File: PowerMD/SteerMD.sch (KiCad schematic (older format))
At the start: 202 parts, among them P1 SWD, P10 OUT_1, P11 ENC_0, P13 ENC_1, P14 I/O_1, P15 OUT_0, P3 CAN, P4 CAN, P5 SERIAL, P6 I/O_0, P7 FAN, P8 BATT_IN, P9 BATT_IN, Q1 MOSFET_N, Q2 MOSFET_N, Q3 MOSFET_N, Q4 MOSFET_N, Q5 MOSFET_N, Q6 MOSFET_N, Q7 MOSFET_N, Q8 MOSFET_N, SW1 RST, SW3 SW0, SW4 SW1, U1 MAX3051, U10 ACS758, U11 POWER_ON, U12 SI8274, U13 ACS758, U14 SI8274, U15 AZ1086H, U16 LOGO, U19 ADRESS, U2 AP3211, U3 STM32F405RG, U4 SI8274, U5 SI8900, U6 ADC_~RST, U7 BD9G101G, U8 SI8274, U9 BD33FA1, Y1 8MHz

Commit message: サーミスタのピンアサインの決定
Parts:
- added C53, C54, C58, C59: 0.1u, Capacitor_SMD:C_0603_1608Metric, symbol SteerMD-rescue:C-Device-MD_Enbarr_x2-rescue-F4_CAN_DCMD-rescue
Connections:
- net Current0: now also U3.25 (PC5/ADC12_IN15); no longer U3.11 (PC3/ADC12_IN13)
- net Current1: now also U3.24 (PC4/ADC12_IN14); no longer U3.10 (PC2/ADC12_IN12)
- net GND: now also C53.2, C54.2, C58.2, C59.2
- net LED0: no longer U3.22 (ADC12_IN6/TIM3_CH1/TIM13_CH1/PA6)
- net LED1: no longer U3.23 (ADC12_IN7/TIM1_CH1N/TIM8_CH1N/TIM14_CH1/TIM3_CH2/PA7)
- net LED2: no longer U3.24 (PC4/ADC12_IN14)
- net LED3: no longer U3.25 (PC5/ADC12_IN15)
- net Motor0L_Tmp: now also U3.8 (PC0/ADC12_IN10), C53.1
- net Motor0R_Tmp: now also U3.9 (PC1/ADC12_IN11), C58.1
- net Motor1L_Tmp: now also U3.10 (PC2/ADC12_IN12), C54.1
- net Motor1R_Tmp: now also U3.11 (PC3/ADC12_IN13), C59.1
- net LED4: no longer names the net of U3.26 (ADC12_IN8/TIM1_CH2N/TIM8_CH2N/TIM3_CH3/PB0)
- removed net Motor1_Tmp: U3.8 (PC0/ADC12_IN10), U3.9 (PC1/ADC12_IN11)
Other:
- moved on the sheet: R52, R67, R68, R69, TH1, TH2, TH3, TH4

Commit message: パワミMD
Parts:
- C34: footprint Capacitor_THT:CP_Radial_D10.0mm_P5.00mm -> Capacitor_THT:C_Radial_D12.5mm_H25.0mm_P5.00mm
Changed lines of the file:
@@
 F 0 "C34" H 10665 971 50  0000 L CNN
 F 1 "1500u" H 10665 880 50  0000 L CNN
-F 2 "Capacitor_THT:CP_Radial_D10.0mm_P5.00mm" H 10550 925 50  0001 C CNN
+F 2 "Capacitor_THT:C_Radial_D12.5mm_H25.0mm_P5.00mm" H 10550 925 50  0001 C CNN
 F 3 "~" H 10550 925 50  0001 C CNN
 	1    10550 925

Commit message: ピン配置王幅変更
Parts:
- added C60: 0.1u, Capacitor_SMD:C_0603_1608Metric, symbol SteerMD-rescue:C-Device-MD_Enbarr_x2-rescue-F4_CAN_DCMD-rescue
- added R70: FILTER, Resistor_SMD:R_0603_1608Metric, symbol SteerMD-rescue:R-Device-MD_Enbarr_x2-rescue-F4_CAN_DCMD-rescue
- added TH5: Thermistor, Capacitor_SMD:C_0603_1608Metric, symbol Device:Thermistor
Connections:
- net +3V3: now also TH5.1
- net ADR_1: no longer U3.4 (PC15/OSC32_OUT)
- net ADR_2: no longer U3.2 (PC13)
- net ADR_4: no longer U3.3 (PC14/OSC32_IN)
- net ADR_8: no longer U3.58 (TIM4_CH1/CAN2_TX/USART1_TX/PB6)
- net Current0: no longer U3.25 (PC5/ADC12_IN15)
- net Current1: no longer U3.24 (PC4/ADC12_IN14)
- net GND: now also C60.2, R70.2
- net Motor0L_Tmp: now also U3.9 (PC1/ADC12_IN11); no longer U3.8 (PC0/ADC12_IN10)
- net Motor0R_Tmp: now also U3.8 (PC0/ADC12_IN10); no longer U3.9 (PC1/ADC12_IN11)
- net Motor1L_Tmp: now also U3.25 (PC5/ADC12_IN15); no longer U3.10 (PC2/ADC12_IN12)
- net Motor1R_Tmp: now also U3.26 (ADC12_IN8/TIM1_CH2N/TIM8_CH2N/TIM3_CH3/PB0); no longer U3.11 (PC3/ADC12_IN13)
- net SW0: no longer U3.27 (ADC12_IN9/TIM1_CH3N/TIM8_CH3N/TIM3_CH4/PB1)
- net SW1: no longer U3.29 (USART3_TX/TIM2_CH3/PB10)
- net PA12: now reaches U3.45 (CAN1_TX/PA12)
- net PA12: now also U6.1
- net PA11: no longer names the net of U3.44 (CAN1_RX/TIM1_CH4/PA11)
- net PA11: no longer U6.1
- net PA15: no longer names the net of U3.50 (TIM2_CH1_ETR/PA15)
- net PA4 renamed IO_0
- net IO_0: no longer U3.20 (ADC12_IN4/PA4)
- net PA5: no longer names the net of U3.21 (ADC12_IN5/TIM2_CH1_ETR/TIM8_CH1N/PA5)
- net PA5: no longer P14.3 (P3)
- new net IO_1: P14.3 (P3)
- new net Substrate_Temp: C60.1, R70.1, TH5.2, U3.20 (ADC12_IN4/PA4)
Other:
- moved on the sheet: C53, C54, C58, C59, R52, R67, R68, R69, TH1, TH2, TH3, TH4

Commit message: MD
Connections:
- net ADR_1: now also U3.21 (ADC12_IN5/TIM2_CH1_ETR/TIM8_CH1N/PA5)
- net ADR_2: now also U3.23 (ADC12_IN7/TIM1_CH1N/TIM8_CH1N/TIM14_CH1/TIM3_CH2/PA7)
- net ADR_4: now also U3.22 (ADC12_IN6/TIM3_CH1/TIM13_CH1/PA6)
- net ADR_8: now also U3.27 (ADC12_IN9/TIM1_CH3N/TIM8_CH3N/TIM3_CH4/PB1)
- net Current0: now also U3.10 (PC2/ADC12_IN12)
- net Current1: now also U3.24 (PC4/ADC12_IN14)
- net LED0: now also U3.50 (TIM2_CH1_ETR/PA15)
- net LED1: now also U3.51 (PC10/UART4_TX/USART3_TX)
- net LED2: now also U3.52 (PC11/UART4_RX/USART3_RX)
- net LED3: now also U3.53 (PC12/UART5_TX)
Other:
- note added: "Filter:10kohm"
- note added: "Filter:3ohm"
- moved on the sheet: C15, C16, C26, C44, C55, D39, D7, D8, D9, P11, P13, P14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

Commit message: MDにモータ駆動用のファンぽーとをつけた
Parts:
- added P2: MOTOR_COOLING, Mizz_lib:XA_4L, symbol SteerMD-rescue:CONN_01X04-conn-MD_Enbarr_x2-rescue-F4_CAN_DCMD-rescue
- added R71, R72: 12, Mizz_lib:R_2812, symbol SteerMD-rescue:R-Device-MD_Enbarr_x2-rescue-F4_CAN_DCMD-rescue
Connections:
- net +12V: now also R71.2, R72.2
- net GND: now also P2.1 (P1), P2.3 (P3)
- net Motor1L_Tmp: no longer U3.25 (PC5/ADC12_IN15)
- net Motor1R_Tmp: now also U3.25 (PC5/ADC12_IN15); no longer U3.26 (ADC12_IN8/TIM1_CH2N/TIM8_CH2N/TIM3_CH3/PB0)
- net TIM4_CH1: now reaches U3.58 (TIM4_CH1/CAN2_TX/USART1_TX/PB6)
- net TIM4_CH1: now also R46.2
- net TIM4_CH2: now reaches U3.59 (USART1_RX/TIM4_CH2/PB7)
- net TIM4_CH2: now also R50.2
- net TIM5_CH1: no longer names the net of U3.14 (UART4_TX/TIM2_CH1_ETR/ADC12_IN0/TIM5_CH1/PA0)
- net TIM5_CH1: no longer R46.2
- net TIM5_CH2: no longer names the net of U3.15 (UART4_RX/ADC12_IN1/TIM5_CH2/TIM2_CH2/PA1)
- net TIM5_CH2: no longer R50.2
- new net: P2.2 (P2), R71.1
- new net: P2.4 (P4), R72.1
- new net Motor1l_Tmp: U3.26 (ADC12_IN8/TIM1_CH2N/TIM8_CH2N/TIM3_CH3/PB0)
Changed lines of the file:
@@
 Text Label 8250 900  2    50   ~ 0
 PA12
-Text Label 6900 6450 0    50   ~ 0
-PWM1_R
-Text Label 6900 6650 0    50   ~ 0
-PWM1_L
 Text Label 6900 6550 0    50   ~ 0
 EN1
@@
 	1    0    0    -1
 $EndComp
-Text Label 5350 9600 2    50   ~ 0
-TIM5_CH2
-Text Label 5350 9700 2    50   ~ 0
-TIM5_CH1
 $Comp
 L SteerMD-rescue:R-Device-MD_Enbarr_x2-rescue-F4_CAN_DCMD-rescue R24
@@
 Text Label 8125 4850 0    50   ~ 0
 SW1
-Text Label 6900 3450 0    50   ~ 0
-TIM5_CH1
-Text Label 6900 3550 0    50   ~ 0
-TIM5_CH2
 $Comp
 L SteerMD-rescue:CONN_01X03-conn-MD_Enbarr_x2-rescue-F4_CAN_DCMD-rescue P14
@@
 Motor0L_Tmp
 Text Label 2500 5650 2    50   ~ 0
-Motor1L_Tmp
-Text Label 6900 5150 0    50   ~ 0
 Motor1R_Tmp
+Text Label 6900 5150 0    50   ~ 0
+Motor1l_Tmp
 $Comp
 L Device:Thermistor TH5
@@
 Text Notes 7675 6050 0    50   ~ 0
 Filter:10kohm
+Text Label 6900 5850 0    50   ~ 0
+TIM4_CH2
+Text Label 6900 5750 0    50   ~ 0
+TIM4_CH1
+Text Label 5350 9600 2    50   ~ 0
+TIM4_CH2
+Text Label 5350 9700 2    50   ~ 0
+TIM4_CH1
+Text Label 6900 6450 0    50   ~ 0
+PWM1_R
+Text Label 6900 6650 0    50   ~ 0
+PWM1_L
+$Comp
+L SteerMD-rescue:+12V-power-MD_Enbarr_x2-rescue-F4_CAN_DCMD-rescue #PWR0166
+U 1 1 5E004D06
+P 7450 9500
+F 0 "#PWR0166" H 7450 9350 50  0001 C CNN
+F 1 "+12V" H 7465 9673 50  0000 C CNN
+F 2 "" H 7450 9500 50  0001 C CNN
+F 3 "" H 7450 9500 50  0001 C CNN
+	1    7450 9500
+	1    0    0    -1
+$EndComp
+$Comp
+L SteerMD-rescue:R-Device-MD_Enbarr_x2-rescue-F4_CAN_DCMD-rescue R71
+U 1 1 5E00731A
+P 7600 9500
+F 0 "R71" V 7393 9500 50  0000 C CNN
+F 1 "12" V 7484 9500 50  0000 C CNN
+F 2 "Mizz_lib:R_2812" V 7530 9500 50  0001 C CNN
+F 3 "~" H 7600 9500 50  0001 C CNN
+	1    7600 9500
+	0    1    1    0
+$EndComp
+$Comp
+L SteerMD-rescue:GND-power-MD_Enbarr_x2-rescue-F4_CAN_DCMD-rescue #PWR0167
+U 1 1 5E008AB5
+P 7775 9400
+F 0 "#PWR0167" H 7775 9150 50  0001 C CNN
+F 1 "GND" H 7780 9227 50  0000 C CNN
+F 2 "" H 7775 9400 50  0001 C CNN
+F 3 "" H 7775 9400 50  0001 C CNN
+	1    7775 9400
+	1    0    0    -1
+$EndComp
+Wire Wire Line
+	7800 9500 7750 9500
+Wire Wire Line
+	7775 9400 7800 9400
+$Comp
+L SteerMD-rescue:R-Device-MD_Enbarr_x2-rescue-F4_CAN_DCMD-rescue R72
+U 1 1 5E080808
+P 7600 9700
+F 0 "R72" V 7393 9700 50  0000 C CNN
+F 1 "12" V 7484 9700 50  0000 C CNN
+F 2 "Mizz_lib:R_2812" V 7530 9700 50  0001 C CNN
+F 3 "~" H 7600 9700 50  0001 C CNN
+	1    7600 9700
+	0    1    1    0
+$EndComp
+$Comp
+L SteerMD-rescue:GND-power-MD_Enbarr_x2-rescue-F4_CAN_DCMD-rescue #PWR0169
+U 1 1 5E080812
+P 7775 9600
+F 0 "#PWR0169" H 7775 9350 50  0001 C CNN
+F 1 "GND" H 7780 9427 50  0000 C CNN
+F 2 "" H 7775 9600 50  0001 C CNN
+F 3 "" H 7775 9600 50  0001 C CNN
+	1    7775 9600
+	1    0    0    -1
+$EndComp
+Wire Wire Line
+	7800 9700 7750 9700
+Wire Wire Line
+	7775 9600 7800 9600
+$Comp
+L SteerMD-rescue:CONN_01X04-conn-MD_Enbarr_x2-rescue-F4_CAN_DCMD-rescue P2
+U 1 1 5E199ED6
+P 8000 9550
+F 0 "P2" H 8078 9591 50  0000 L CNN
+F 1 "MOTOR_COOLING" H 8078 9500 50  0000 L CNN
+F 2 "Mizz_lib:XA_4L" H 8000 9550 50  0001 C CNN
+F 3 "" H 8000 9550 50  0000 C CNN
+	1    8000 9550
+	1    0    0    -1
+$EndComp
+Wire Wire Line
+	7450 9500 7450 9700
+Connection ~ 7450 9500
 $EndSCHEMATC

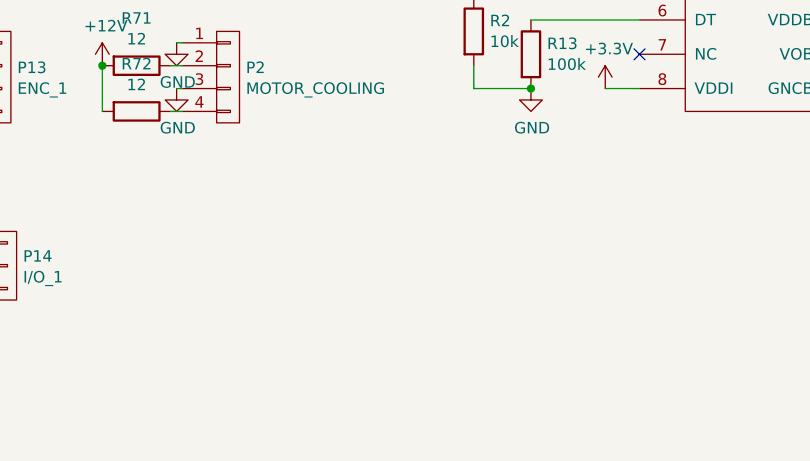
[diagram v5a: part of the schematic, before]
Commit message: パワー系の配線完了かな
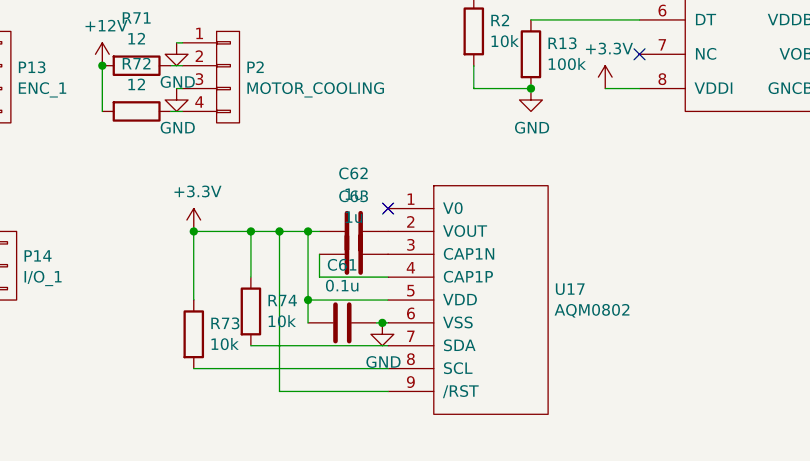
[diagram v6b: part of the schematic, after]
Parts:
- added C61: 0.1u, Capacitor_SMD:C_0603_1608Metric, symbol SteerMD-rescue:C-Device-MD_Enbarr_x2-rescue-F4_CAN_DCMD-rescue
- added C62, C63: 1u, Capacitor_SMD:C_0603_1608Metric, symbol SteerMD-rescue:C-Device-MD_Enbarr_x2-rescue-F4_CAN_DCMD-rescue
- added R73, R74: 10k, Resistor_SMD:R_0603_1608Metric, symbol SteerMD-rescue:R-Device-MD_Enbarr_x2-rescue-F4_CAN_DCMD-rescue
- added U17: AQM0802, Mizz_lib:AQM0802_original, symbol Miz:AQM1602
- D1, D11, D13, D14, D19, D2, D20, D3: footprint Diode_SMD:D_0603_1608Metric -> Mizz_lib:1608_WP
- R19, R20, R28, R29, R55, R56, R58, R59: footprint Resistor_SMD:R_0603_1608Metric -> Mizz_lib:1608_WP
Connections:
- net +3V3: now also C61.2, C62.2, R73.1, R74.1, U17.5 (VDD), U17.9 (/RST)
- net GND: now also C61.1, U17.6 (VSS)
- new net: C62.1, U17.2 (VOUT)
- new net: C63.1, U17.3 (CAP1N)
- new net: C63.2, U17.4 (CAP1P)
- new net: R74.2, U17.7 (SDA)
- new net: R73.2, U17.8 (SCL)
- no-connect marks 17 -> 18

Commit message: 2019/12/31
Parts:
- added C64: 100u, Capacitor_THT:CP_Radial_D5.0mm_P2.50mm, symbol SteerMD-rescue:CP1-Device-MD_Enbarr_x2-rescue-F4_CAN_DCMD-rescue
- U2: value AP3211 -> BD9G101
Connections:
- net +12P: now also C64.1
- net GND: now also D39.1 (K), D7.1 (K), D8.1 (K), D9.1 (K); no longer R51.2, R6.2, R7.2, R8.2
- net GNDPWR: now also C64.2
- net LED0: now also R6.1; no longer D7.2 (A)
- net LED1: now also R7.1; no longer D8.2 (A)
- net LED2: now also R8.1; no longer D9.2 (A)
- net LED3: now also R51.1; no longer D39.2 (A)
- new net: D39.2 (A), R51.2
- new net: D7.2 (A), R6.2
- new net: D8.2 (A), R7.2
- new net: D9.2 (A), R8.2
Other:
- moved on the sheet: C29, C32, D39, D7, D8, D9, R51, R6, R7, R8, U9
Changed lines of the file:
@@
 L SteerMD-rescue:LED-Device-MD_Enbarr_x2-rescue-F4_CAN_DCMD-rescue D7
 U 1 1 5E3557C3
-P 1600 10125
-F 0 "D7" V 1639 10007 50  0000 R CNN
-F 1 "EMG1" V 1548 10007 50  0000 R CNN
-F 2 "LED_SMD:LED_0603_1608Metric" H 1600 10125 50  0001 C CNN
-F 3 "~" H 1600 10125 50  0001 C CNN
-	1    1600 10125
+P 1600 10425
+F 0 "D7" V 1639 10307 50  0000 R CNN
+F 1 "EMG1" V 1548 10307 50  0000 R CNN
+F 2 "LED_SMD:LED_0603_1608Metric" H 1600 10425 50  0001 C CNN
+F 3 "~" H 1600 10425 50  0001 C CNN
+	1    1600 10425
 	0    -1   -1   0
 $EndComp
@@
 L SteerMD-rescue:R-Device-MD_Enbarr_x2-rescue-F4_CAN_DCMD-rescue R7
 U 1 1 5E356E52
-P 1975 10425
-F 0 "R7" H 2045 10471 50  0000 L CNN
-F 1 "330" H 2045 10380 50  0000 L CNN
-F 2 "Resistor_SMD:R_0603_1608Metric" V 1905 10425 50  0001 C CNN
-F 3 "~" H 1975 10425 50  0001 C CNN
-	1    1975 10425
+P 1975 10125
+F 0 "R7" H 2045 10171 50  0000 L CNN
+F 1 "330" H 2045 10080 50  0000 L CNN
+F 2 "Resistor_SMD:R_0603_1608Metric" V 1905 10125 50  0001 C CNN
+F 3 "~" H 1975 10125 50  0001 C CNN
+	1    1975 10125
 	1    0    0    -1
 $EndComp
@@
 L SteerMD-rescue:LED-Device-MD_Enbarr_x2-rescue-F4_CAN_DCMD-rescue D8
 U 1 1 5E356E5C
-P 1975 10125
-F 0 "D8" V 2014 10008 50  0000 R CNN
-F 1 "BUS1" V 1923 10008 50  0000 R CNN
-F 2 "LED_SMD:LED_0603_1608Metric" H 1975 10125 50  0001 C CNN
-F 3 "~" H 1975 10125 50  0001 C CNN
-	1    1975 10125
+P 1975 10425
+F 0 "D8" V 2014 10308 50  0000 R CNN
+F 1 "BUS1" V 1923 10308 50  0000 R CNN
+F 2 "LED_SMD:LED_0603_1608Metric" H 1975 10425 50  0001 C CNN
+F 3 "~" H 1975 10425 50  0001 C CNN
+	1    1975 10425
 	0    -1   -1   0
 $EndComp
@@
 L SteerMD-rescue:R-Device-MD_Enbarr_x2-rescue-F4_CAN_DCMD-rescue R8
 U 1 1 5E35F947
-P 2325 10425
-F 0 "R8" H 2395 10471 50  0000 L CNN
-F 1 "330" H 2395 10380 50  0000 L CNN
-F 2 "Resistor_SMD:R_0603_1608Metric" V 2255 10425 50  0001 C CNN
-F 3 "~" H 2325 10425 50  0001 C CNN
-	1    2325 10425
+P 2325 10125
+F 0 "R8" H 2395 10171 50  0000 L CNN
+F 1 "330" H 2395 10080 50  0000 L CNN
+F 2 "Resistor_SMD:R_0603_1608Metric" V 2255 10125 50  0001 C CNN
+F 3 "~" H 2325 10125 50  0001 C CNN
+	1    2325 10125
 	1    0    0    -1
 $EndComp
@@
 L SteerMD-rescue:LED-Device-MD_Enbarr_x2-rescue-F4_CAN_DCMD-rescue D9
 U 1 1 5E35F951
-P 2325 10125
-F 0 "D9" V 2364 10007 50  0000 R CNN
-F 1 "EMG0" V 2273 10007 50  0000 R CNN
-F 2 "LED_SMD:LED_0603_1608Metric" H 2325 10125 50  0001 C CNN
-F 3 "~" H 2325 10125 50  0001 C CNN
-	1    2325 10125
+P 2325 10425
+F 0 "D9" V 2364 10307 50  0000 R CNN
+F 1 "EMG0" V 2273 10307 50  0000 R CNN
+F 2 "LED_SMD:LED_0603_1608Metric" H 2325 10425 50  0001 C CNN
+F 3 "~" H 2325 10425 50  0001 C CNN
+	1    2325 10425
 	0    -1   -1   0
 $EndComp
@@
 P 2250 1500
 F 0 "U2" H 2250 1965 50  0000 C CNN
-F 1 "AP3211" H 2250 1874 50  0000 C CNN
+F 1 "BD9G101" H 2250 1874 50  0000 C CNN
 F 2 "Package_SO:TSOP-6_1.65x3.05mm_P0.95mm" H 2250 1500 50  0001 C CNN
 F 3 "" H 2250 1500 50  0001 C CNN
@@
 L SteerMD-rescue:R-Device-MD_Enbarr_x2-rescue-F4_CAN_DCMD-rescue R6
 U 1 1 5E354377
-P 1600 10425
-F 0 "R6" H 1670 10471 50  0000 L CNN
-F 1 "330" H 1670 10380 50  0000 L CNN
-F 2 "Resistor_SMD:R_0603_1608Metric" V 1530 10425 50  0001 C CNN
-F 3 "~" H 1600 10425 50  0001 C CNN
-	1    1600 10425
+P 1600 10125
+F 0 "R6" H 1670 10171 50  0000 L CNN
+F 1 "330" H 1670 10080 50  0000 L CNN
+F 2 "Resistor_SMD:R_0603_1608Metric" V 1530 10125 50  0001 C CNN
+F 3 "~" H 1600 10125 50  0001 C CNN
+	1    1600 10125
 	1    0    0    -1
 $EndComp
@@
 L SteerMD-rescue:LED-Device-MD_Enbarr_x2-rescue-F4_CAN_DCMD-rescue D39
 U 1 1 5DA17808
-P 2700 10125
-F 0 "D39" V 2739 10007 50  0000 R CNN
-F 1 "BUS0" V 2648 10007 50  0000 R CNN
-F 2 "LED_SMD:LED_0603_1608Metric" H 2700 10125 50  0001 C CNN
-F 3 "~" H 2700 10125 50  0001 C CNN
-	1    2700 10125
+P 2700 10425
+F 0 "D39" V 2739 10307 50  0000 R CNN
+F 1 "BUS0" V 2648 10307 50  0000 R CNN
+F 2 "LED_SMD:LED_0603_1608Metric" H 2700 10425 50  0001 C CNN
+F 3 "~" H 2700 10425 50  0001 C CNN
+	1    2700 10425
 	0    -1   -1   0
 $EndComp
@@
 L SteerMD-rescue:R-Device-MD_Enbarr_x2-rescue-F4_CAN_DCMD-rescue R51
 U 1 1 5DA1783A
-P 2700 10425
-F 0 "R51" H 2770 10471 50  0000 L CNN
-F 1 "330" H 2770 10380 50  0000 L CNN
-F 2 "Resistor_SMD:R_0603_1608Metric" V 2630 10425 50  0001 C CNN
-F 3 "~" H 2700 10425 50  0001 C CNN
-	1    2700 10425
+P 2700 10125
+F 0 "R51" H 2770 10171 50  0000 L CNN
+F 1 "330" H 2770 10080 50  0000 L CNN
+F 2 "Resistor_SMD:R_0603_1608Metric" V 2630 10125 50  0001 C CNN
+F 3 "~" H 2700 10125 50  0001 C CNN
+	1    2700 10125
 	1    0    0    -1
 $EndComp
@@
 	1    0    0    -1
 $EndComp
-Connection ~ 14475 4450
+Connection ~ 14800 4450
 Wire Wire Line
-	14025 4450 14475 4450
+	14350 4450 14800 4450
 Wire Wire Line
-	14025 4375 14025 4450
+	14350 4375 14350 4450
 Wire Wire Line
-	14025 4000 14025 4075
+	14350 4000 14350 4075
 Wire Wire Line
-	14775 4450 14625 4450
-Connection ~ 14775 4450
-Connection ~ 14625 4450
+	15100 4450 14950 4450
+Connection ~ 15100 4450
+Connection ~ 14950 4450
 Wire Wire Line
-	15125 4450 14775 4450
+	15450 4450 15100 4450
 Wire Wire Line
-	15125 4375 15125 4450
+	15450 4375 15450 4450
 Wire Wire Line
-	15125 4000 15125 4075
+	15450 4000 15450 4075
 Wire Wire Line
-	14625 4450 14475 4450
+	14950 4450 14800 4450
 $Comp
 L SteerMD-rescue:GNDPWR-power-MD_Enbarr_x2-rescue-F4_CAN_DCMD-rescue #PWR069
 U 1 1 5E4ED781
-P 14625 4450
-F 0 "#PWR069" H 14625 4250 50  0001 C CNN
-F 1 "GNDPWR" H 14629 4296 50  0000 C CNN
-F 2 "" H 14625 4400 50  0001 C CNN
-F 3 "" H 14625 4400 50  0001 C CNN
-	1    14625 4450
+P 14950 4450
+F 0 "#PWR069" H 14950 4250 50  0001 C CNN
+F 1 "GNDPWR" H 14954 4296 50  0000 C CNN
+F 2 "" H 14950 4400 50  0001 C CNN
+F 3 "" H 14950 4400 50  0001 C CNN
+	1    14950 4450
 	1    0    0    -1
 $EndComp
-Connection ~ 15125 4000
+Connection ~ 15450 4000
 $Comp
 L SteerMD-rescue:+3.3VP-power-MD_Enbarr_x2-rescue-F4_CAN_DCMD-rescue #PWR071
 U 1 1 5E4E26F2
-P 15125 4000
-F 0 "#PWR071" H 15275 3950 50  0001 C CNN
-F 1 "+3.3VP" H 15145 4143 50  0000 C CNN
-F 2 "" H 15125 4000 50  0001 C CNN
-F 3 "" H 15125 4000 50  0001 C CNN
-	1    15125 4000
+P 15450 4000
+F 0 "#PWR071" H 15600 3950 50  0001 C CNN
+F 1 "+3.3VP" H 15470 4143 50  0000 C CNN
+F 2 "" H 15450 4000 50  0001 C CNN
+F 3 "" H 15450 4000 50  0001 C CNN
+	1    15450 4000
 	1    0    0    -1
 $EndComp
@@
 L SteerMD-rescue:C-Device-MD_Enbarr_x2-rescue-F4_CAN_DCMD-rescue C32
 U 1 1 5E4E0B6F
-P 15125 4225
-F 0 "C32" H 15240 4271 50  0000 L CNN
-F 1 "4.7u" H 15240 4180 50  0000 L CNN
-F 2 "Capacitor_SMD:C_0805_2012Metric" H 15163 4075 50  0001 C CNN
-F 3 "~" H 15125 4225 50  0001 C CNN
-	1    15125 4225
+P 15450 4225
+F 0 "C32" H 15565 4271 50  0000 L CNN
+F 1 "4.7u" H 15565 4180 50  0000 L CNN
+F 2 "Capacitor_SMD:C_0805_2012Metric" H 15488 4075 50  0001 C CNN
+F 3 "~" H 15450 4225 50  0001 C CNN
+	1    15450 4225
 	1    0    0    -1
 $EndComp
 Wire Wire Line
-	14025 4000 14125 4000
-Connection ~ 14025 4000
-Connection ~ 13950 4000
-Wire Wire Line
-	13950 4000 14025 4000
+	14350 4000 14450 4000
 $Comp
 L Miz:BD33FA1 U9
 U 1 1 5E4CACF9
-P 14625 4050
-F 0 "U9" H 14625 4465 50  0000 C CNN
-F 1 "BD33FA1" H 14625 4374 50  0000 C CNN
-F 2 "Package_TO_SOT_SMD:SOT-89-3" H 14625 4150 50  0001 C CNN
-F 3 "" H 14625 4150 50  0001 C CNN
-	1    14625 4050
+P 14950 4050
+F 0 "U9" H 14950 4465 50  0000 C CNN
+F 1 "BD33FA1" H 14950 4374 50  0000 C CNN
+F 2 "Package_TO_SOT_SMD:SOT-89-3" H 14950 4150 50  0001 C CNN
+F 3 "" H 14950 4150 50  0001 C CNN
+	1    14950 4050
 	1    0    0    -1
 $EndComp
@@
 L SteerMD-rescue:C-Device-MD_Enbarr_x2-rescue-F4_CAN_DCMD-rescue C29
 U 1 1 5E4C8A81
-P 14025 4225
-F 0 "C29" H 14140 4271 50  0000 L CNN
-F 1 "4.7u" H 14140 4180 50  0000 L CNN
-F 2 "Capacitor_SMD:C_0805_2012Metric" H 14063 4075 50  0001 C CNN
-F 3 "~" H 14025 4225 50  0001 C CNN
-	1    14025 4225
+P 14350 4225
+F 0 "C29" H 14465 4271 50  0000 L CNN
+F 1 "4.7u" H 14465 4180 50  0000 L CNN
+F 2 "Capacitor_SMD:C_0805_2012Metric" H 14388 4075 50  0001 C CNN
+F 3 "~" H 14350 4225 50  0001 C CNN
+	1    14350 4225
 	1    0    0    -1
 $EndComp
@@
 L SteerMD-rescue:+12P-power-MD_Enbarr_x2-rescue-F4_CAN_DCMD-rescue #PWR067
 U 1 1 5E43C009
-P 13950 4000
-F 0 "#PWR067" H 13950 3850 50  0001 C CNN
-F 1 "+12P" H 13965 4173 50  0000 C CNN
-F 2 "" H 13950 4000 50  0001 C CNN
-F 3 "" H 13950 4000 50  0001 C CNN
-	1    13950 4000
+P 14350 4000
+F 0 "#PWR067" H 14350 3850 50  0001 C CNN
+F 1 "+12P" H 14365 4173 50  0000 C CNN
+F 2 "" H 14350 4000 50  0001 C CNN
+F 3 "" H 14350 4000 50  0001 C CNN
+	1    14350 4000
 	1    0    0    -1
 $EndComp
@@
 Wire Wire Line
 	8225 10225 8350 10225
+$Comp
+L SteerMD-rescue:CP1-Device-MD_Enbarr_x2-rescue-F4_CAN_DCMD-rescue C64
+U 1 1 5E0F3249
+P 13950 4200
+F 0 "C64" H 14065 4246 50  0000 L CNN
+F 1 "100u" H 14065 4155 50  0000 L CNN
+F 2 "Capacitor_THT:CP_Radial_D5.0mm_P2.50mm" H 13950 4200 50  0001 C CNN
+F 3 "~" H 13950 4200 50  0001 C CNN
+	1    13950 4200
+	1    0    0    -1
+$EndComp
+Wire Wire Line
+	13950 4350 13950 4450
+Wire Wire Line
+	13950 4450 14350 4450
+Connection ~ 14350 4450
+Connection ~ 14350 4000
+Wire Wire Line
+	14350 4000 13950 4000
+Wire Wire Line
+	13950 4000 13950 4050
+Connection ~ 13950 4000
 $EndSCHEMATC

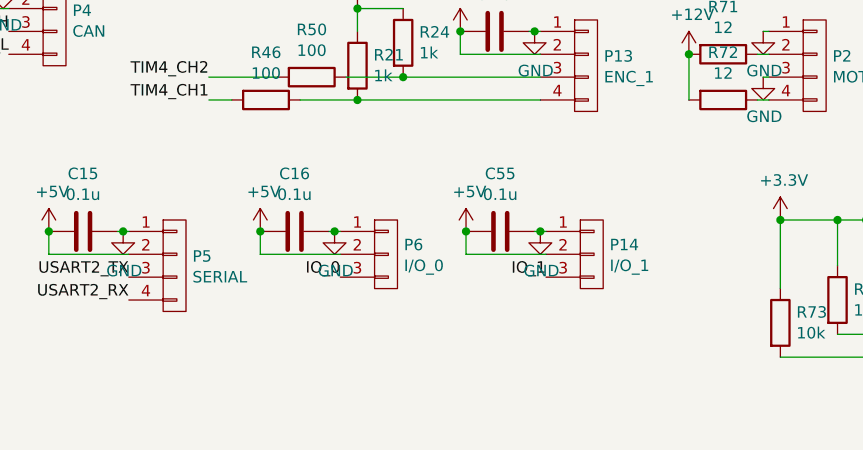
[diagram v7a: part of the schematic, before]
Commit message: また回路図的に仕様(?)を変更した
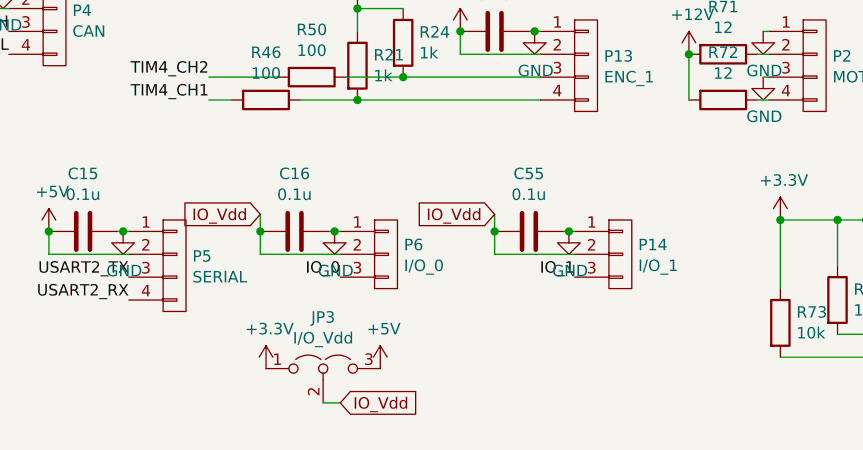
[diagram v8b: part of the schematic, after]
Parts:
- added JP3: I/O_Vdd, Mizz_lib:SW_Micro_SPST, symbol Jumper:Jumper_3_Open
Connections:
- net +3V3: now also JP3.1 (A)
- net +5V: now also JP3.3 (B); no longer C16.2, C55.2, P14.2 (P2), P6.2 (P2)
- new net IO_Vdd: C16.2, C55.2, JP3.2 (C), P14.2 (P2), P6.2 (P2)
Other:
- moved on the sheet: C55, P14
